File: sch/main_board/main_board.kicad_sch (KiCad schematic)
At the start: 58 parts, among them J1 BVCC, J13 5V_GND, J14 IO23, J15 IO22, J16 IO1, J17 IO3, J18 IO21, J2 BGND, J21 5V, J22 TX2, J23 RX2, J24 12V_CUT2, J25 12V_CUT, J26 DC 12V, J27 DC 5V, J3 3.3V, J30 5V_CUT, J4 PWR_MOTOR_L, J5 PWR_MOTOR_R, J6 CUT_LOAD, J7 MOTOR_L, J8 MOTOR_R, J9 EN, Q1 BC847, Q2 K4145, Q3 K4145, Q4 BC847, Q5 K4145, Q6 BC847, Q7 K4145, Q8 BC847, Q9 K4145

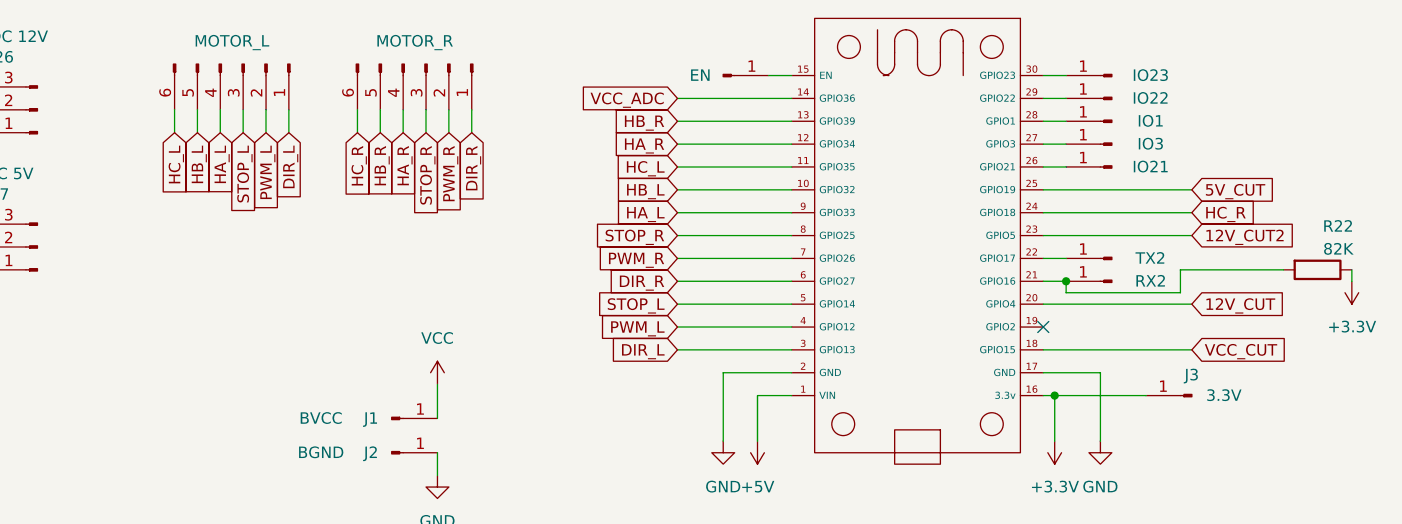
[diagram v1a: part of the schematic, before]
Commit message: Swap the motors. Simply because it easier to connect
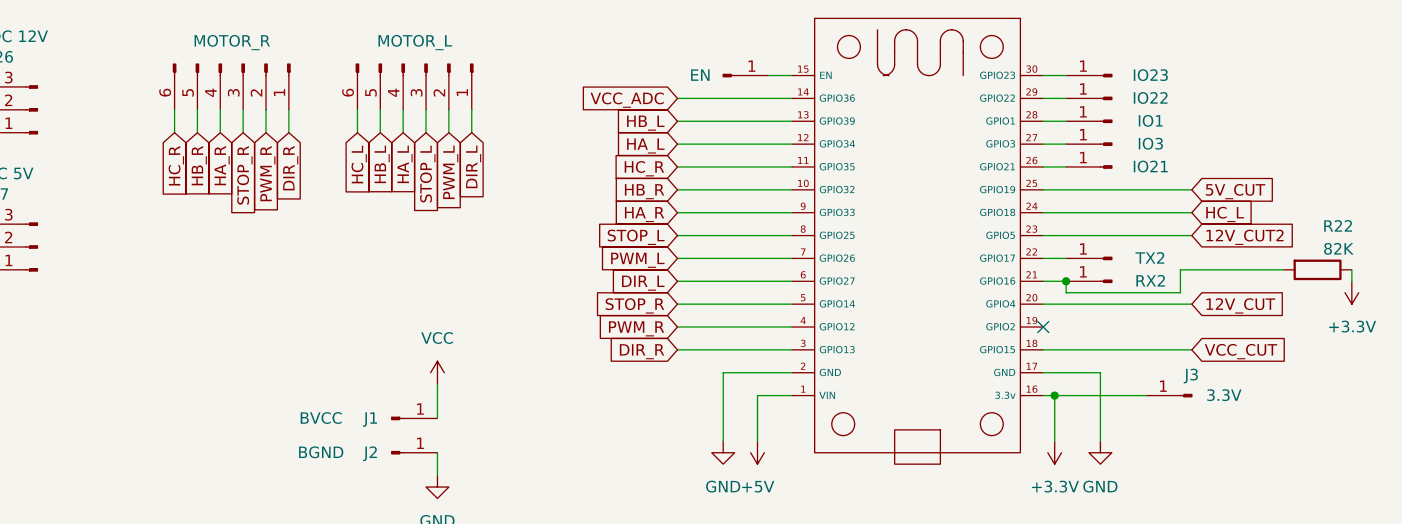
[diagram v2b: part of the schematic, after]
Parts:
- J7: value MOTOR_L -> MOTOR_R
- J8: value MOTOR_R -> MOTOR_L
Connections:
- net DIR_L: now also J8.1 (Pin_1), U1.6 (GPIO27); no longer J7.1 (Pin_1), U1.3 (GPIO13)
- net DIR_R: now also J7.1 (Pin_1), U1.3 (GPIO13); no longer J8.1 (Pin_1), U1.6 (GPIO27)
- net HA_L: now also J8.4 (Pin_4), U1.12 (GPIO34); no longer J7.4 (Pin_4), U1.9 (GPIO33)
- net HA_R: now also J7.4 (Pin_4), U1.9 (GPIO33); no longer J8.4 (Pin_4), U1.12 (GPIO34)
- net HB_L: now also J8.5 (Pin_5), U1.13 (GPIO39); no longer J7.5 (Pin_5), U1.10 (GPIO32)
- net HB_R: now also J7.5 (Pin_5), U1.10 (GPIO32); no longer J8.5 (Pin_5), U1.13 (GPIO39)
- net HC_L: now also J8.6 (Pin_6), U1.24 (GPIO18); no longer J7.6 (Pin_6), U1.11 (GPIO35)
- net HC_R: now also J7.6 (Pin_6), U1.11 (GPIO35); no longer J8.6 (Pin_6), U1.24 (GPIO18)
- net PWM_L: now also J8.2 (Pin_2), U1.7 (GPIO26); no longer J7.2 (Pin_2), U1.4 (GPIO12)
- net PWM_R: now also J7.2 (Pin_2), U1.4 (GPIO12); no longer J8.2 (Pin_2), U1.7 (GPIO26)
- net STOP_L: now also J8.3 (Pin_3), U1.8 (GPIO25); no longer J7.3 (Pin_3), U1.5 (GPIO14)
- net STOP_R: now also J7.3 (Pin_3), U1.5 (GPIO14); no longer J8.3 (Pin_3), U1.8 (GPIO25)
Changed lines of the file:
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@@
 		)
 	)
-	(global_label "HA_R"
+	(global_label "HA_L"
 		(shape input)
 		(at 205.74 29.21 180)
@@
 		)
 		(property "Intersheetrefs" "${INTERSHEET_REFS}"
-			(at 198.0981 29.21 0)
+			(at 198.34 29.21 0)
 			(effects
 				(font
@@
 		)
 	)
-	(global_label "PWM_R"
+	(global_label "PWM_L"
 		(shape input)
 		(at 180.34 27.94 270)
@@
 		)
 		(property "Intersheetrefs" "${INTERSHEET_REFS}"
-			(at 180.34 37.3356 90)
+			(at 180.34 37.0937 90)
 			(effects
 				(font
@@
 		)
 	)
-	(global_label "HC_R"
+	(global_label "HC_L"
 		(shape input)
 		(at 262.89 36.83 0)
@@
 		)
 		(property "Intersheetrefs" "${INTERSHEET_REFS}"
-			(at 270.7133 36.83 0)
+			(at 270.4714 36.83 0)
 			(effects
 				(font
@@
 		)
 	)
-	(global_label "DIR_R"
+	(global_label "DIR_L"
 		(shape input)
 		(at 182.88 27.94 270)
@@
 		)
 		(property "Intersheetrefs" "${INTERSHEET_REFS}"
-			(at 182.88 36.3076 90)
+			(at 182.88 36.0657 90)
 			(effects
 				(font
@@
 		)
 	)
-	(global_label "HC_L"
+	(global_label "HC_R"
 		(shape input)
 		(at 205.74 31.75 180)
@@
 		)
 		(property "Intersheetrefs" "${INTERSHEET_REFS}"
-			(at 198.1586 31.75 0)
+			(at 197.9167 31.75 0)
 			(effects
 				(font
@@
 		)
 	)
-	(global_label "HC_L"
+	(global_label "HC_R"
 		(shape input)
 		(at 149.86 27.94 270)
@@
 		)
 		(property "Intersheetrefs" "${INTERSHEET_REFS}"
-			(at 149.86 35.5214 90)
+			(at 149.86 35.7633 90)
 			(effects
 				(font
@@
 		)
 	)
-	(global_label "PWM_L"
+	(global_label "PWM_R"
 		(shape input)
 		(at 205.74 49.53 180)
@@
 		)
 		(property "Intersheetrefs" "${INTERSHEET_REFS}"
-			(at 196.5863 49.53 0)
+			(at 196.3444 49.53 0)
 			(effects
 				(font
@@
 		)
 	)
-	(global_label "HB_R"
+	(global_label "HB_L"
 		(shape input)
 		(at 205.74 26.67 180)
@@
 		)
 		(property "Intersheetrefs" "${INTERSHEET_REFS}"
-			(at 197.9167 26.67 0)
+			(at 198.1586 26.67 0)
 			(effects
 				(font
@@
 		)
 	)
-	(global_label "PWM_R"
+	(global_label "PWM_L"
 		(shape input)
 		(at 205.74 41.91 180)
@@
 		)
 		(property "Intersheetrefs" "${INTERSHEET_REFS}"
-			(at 196.3444 41.91 0)
+			(at 196.5863 41.91 0)
 			(effects
 				(font
@@
 		)
 	)
-	(global_label "DIR_L"
+	(global_label "DIR_R"
 		(shape input)
 		(at 162.56 27.94 270)
@@
 		)
 		(property "Intersheetrefs" "${INTERSHEET_REFS}"
-			(at 162.56 36.0657 90)
+			(at 162.56 36.3076 90)
 			(effects
 				(font
@@
 		)
 	)
-	(global_label "HA_L"
+	(global_label "HA_R"
 		(shape input)
 		(at 205.74 36.83 180)
@@
 		)
 		(property "Intersheetrefs" "${INTERSHEET_REFS}"
-			(at 198.34 36.83 0)
+			(at 198.0981 36.83 0)
 			(effects
 				(font
@@
 		)
 	)
-	(global_label "HA_R"
+	(global_label "HA_L"
 		(shape input)
 		(at 175.26 27.94 270)
@@
 		)
 		(property "Intersheetrefs" "${INTERSHEET_REFS}"
-			(at 175.26 35.5819 90)
+			(at 175.26 35.34 90)
 			(effects
 				(font
@@
 		)
 	)
-	(global_label "HB_R"
+	(global_label "HB_L"
 		(shape input)
 		(at 172.72 27.94 270)
@@
 		)
 		(property "Intersheetrefs" "${INTERSHEET_REFS}"
-			(at 172.72 35.7633 90)
+			(at 172.72 35.5214 90)
 			(effects
 				(font
@@
 		)
 	)
-	(global_label "HB_L"
+	(global_label "HB_R"
 		(shape input)
 		(at 205.74 34.29 180)
@@
 		)
 		(property "Intersheetrefs" "${INTERSHEET_REFS}"
-			(at 198.1586 34.29 0)
+			(at 197.9167 34.29 0)
 			(effects
 				(font
@@
 		)
 	)
-	(global_label "STOP_R"
+	(global_label "STOP_L"
 		(shape input)
 		(at 177.8 27.94 270)
@@
 		)
 		(property "Intersheetrefs" "${INTERSHEET_REFS}"
-			(at 177.8 37.9404 90)
+			(at 177.8 37.6985 90)
 			(effects
 				(font
@@
 		)
 	)
-	(global_label "STOP_L"
+	(global_label "STOP_R"
 		(shape input)
 		(at 205.74 46.99 180)
@@
 		)
 		(property "Intersheetrefs" "${INTERSHEET_REFS}"
-			(at 195.9815 46.99 0)
+			(at 195.7396 46.99 0)
 			(effects
 				(font
@@
 		)
 	)
-	(global_label "HB_L"
+	(global_label "HB_R"
 		(shape input)
 		(at 152.4 27.94 270)
@@
 		)
 		(property "Intersheetrefs" "${INTERSHEET_REFS}"
-			(at 152.4 35.5214 90)
+			(at 152.4 35.7633 90)
 			(effects
 				(font
@@
 		)
 	)
-	(global_label "PWM_L"
+	(global_label "PWM_R"
 		(shape input)
 		(at 160.02 27.94 270)
@@
 		)
 		(property "Intersheetrefs" "${INTERSHEET_REFS}"
-			(at 160.02 37.0937 90)
+			(at 160.02 37.3356 90)
 			(effects
 				(font
@@
 		)
 	)
-	(global_label "DIR_R"
+	(global_label "DIR_L"
 		(shape input)
 		(at 205.74 44.45 180)
@@
 		)
 		(property "Intersheetrefs" "${INTERSHEET_REFS}"
-			(at 197.3724 44.45 0)
+			(at 197.6143 44.45 0)
 			(effects
 				(font
@@
 		)
 	)
-	(global_label "STOP_R"
+	(global_label "STOP_L"
 		(shape input)
 		(at 205.74 39.37 180)
@@
 		)
 		(property "Intersheetrefs" "${INTERSHEET_REFS}"
-			(at 195.7396 39.37 0)
+			(at 195.9815 39.37 0)
 			(effects
 				(font
@@
 		)
 	)
-	(global_label "STOP_L"
+	(global_label "STOP_R"
 		(shape input)
 		(at 157.48 27.94 270)
@@
 		)
 		(property "Intersheetrefs" "${INTERSHEET_REFS}"
-			(at 157.48 37.6985 90)
+			(at 157.48 37.9404 90)
 			(effects
 				(font
@@
 		)
 	)
-	(global_label "HC_R"
+	(global_label "HC_L"
 		(shape input)
 		(at 170.18 27.94 270)
@@
 		)
 		(property "Intersheetrefs" "${INTERSHEET_REFS}"
-			(at 170.18 35.7633 90)
+			(at 170.18 35.5214 90)
 			(effects
 				(font
@@
 		)
 	)
-	(global_label "HA_L"
+	(global_label "HA_R"
 		(shape input)
 		(at 154.94 27.94 270)
@@
 		)
 		(property "Intersheetrefs" "${INTERSHEET_REFS}"
-			(at 154.94 35.34 90)
+			(at 154.94 35.5819 90)
 			(effects
 				(font
@@
 		)
 	)
-	(global_label "DIR_L"
+	(global_label "DIR_R"
 		(shape input)
 		(at 205.74 52.07 180)
@@
 		)
 		(property "Intersheetrefs" "${INTERSHEET_REFS}"
-			(at 197.6143 52.07 0)
+			(at 197.3724 52.07 0)
 			(effects
 				(font
@@
 			)
 		)
-		(property "Value" "MOTOR_R"
+		(property "Value" "MOTOR_L"
 			(at 176.53 17.78 90)
 			(effects
@@
 			)
 		)
-		(property "Value" "MOTOR_L"
+		(property "Value" "MOTOR_R"
 			(at 156.21 17.78 90)
 			(effects

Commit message: Final scheme changes before production
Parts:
- removed C1: 1uf, Capacitor_SMD:C_0805_2012Metric_Pad1.18x1.45mm_HandSolder, symbol Device:C
- removed D1, D2: D, Diode_SMD:D_SMA_Handsoldering, symbol Device:D
- removed Q1, Q4, Q6, Q8: BC847, Package_TO_SOT_SMD:SOT-23, symbol Transistor_BJT:BC847
- removed Q2, Q3, Q5, Q7, Q9: K4145, Package_TO_SOT_THT:TO-220-3_Vertical, symbol Transistor_FET:Q_NMOS_GDS
- removed R15: 10K, Resistor_SMD:R_0805_2012Metric, symbol Device:R
- removed R16, R17, R2: 100K, Resistor_SMD:R_0805_2012Metric, symbol Device:R
- removed R18: 680, Resistor_SMD:R_0805_2012Metric, symbol Device:R
- removed R21: 100, Resistor_SMD:R_0805_2012Metric, symbol Device:R
- added D1, D2: 5.1, Diode_THT:D_5W_P12.70mm_Horizontal, symbol Device:D_Zener
- added D3, D4, D5, D6: D, Diode_SMD:D_2010_5025Metric_Pad1.52x2.65mm_HandSolder, symbol Device:D
- added Q1, Q2, Q3, Q4, Q5: IRF4905, Package_TO_SOT_THT:TO-220-3_Vertical, symbol Transistor_FET:Q_PMOS_GDS
- added R3: 820, Resistor_SMD:R_0805_2012Metric, symbol Device:R
- added U2, U3, U4, U5: EL817, Package_DIP:SMDIP-4_W9.53mm, symbol Isolator:EL817
- R1: value 10K -> 20K
- R10: value 680 -> 1
- R11: value 10K -> 1
- R12, R13: value 100K -> 680
- R2: renamed from R3; value 100K -> 68K
- R4: value 680 -> 820
- R5: value 1 -> 68K
- R6: value 1 -> 820
- R7: value 10K -> 68K
- R8: value 100K -> 820
- R9: value 100K -> 68K
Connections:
- net +12V: now also Q2.3 (S), Q3.3 (S); no longer J24.2 (Pin_2), J25.2 (Pin_2)
- net +3.3V: no longer R12.2, R8.2
- net +5V: now also Q4.3 (S); no longer J21.1 (Pin_1), J30.2 (Pin_2)
- net 12V_CUT: now also R4.2; no longer R11.1
- net 12V_CUT2: now also R6.2
- net 5V_CUT: now also R8.2; no longer R7.1
- net GND: now also J13.1 (Pin_1), J24.1 (Pin_1), J25.1 (Pin_1), J26.2 (Pin_2), J27.2 (Pin_2), J30.1 (Pin_1), J4.1 (Pin_1), J5.1 (Pin_1), J6.1 (Pin_1), R1.1, D3.2 (A), D4.2 (A), D5.2 (A), D6.2 (A), U2.2, U3.2, U3.3, U4.2, U4.3, U5.2, U5.3; no longer J26.1 (Pin_1), J27.1 (Pin_1)
- net VCC: now also J26.1 (Pin_1), J27.1 (Pin_1), R2.2, R5.2, R7.2, R9.2, D1.1 (K), Q1.3 (S), Q5.3 (S); no longer J26.2 (Pin_2), J27.2 (Pin_2), J4.2 (Pin_2), J5.2 (Pin_2), J6.2 (Pin_2)
- net VCC_CUT: now also R3.2; no longer R1.1
- net at R8.1: now also U5.1; no longer R7.2
- net at R12.1: now also Q4.1 (G); no longer R11.2
- net MF_GND: now reaches R1.2
- net MF_GND: now also D2.2 (A), U2.3
- net at R4.1: now also U3.1; no longer R2.1
- net at R14.1: now also Q3.1 (G); no longer R13.1
- net at R14.2: now also R7.1, U4.4
- net at R9.1: now also R12.2, U5.4; no longer R10.1
- net at R10.2: now also R11.2, R2.1, U2.4
- removed net MF_VCC: R13.2, R2.2, R9.2
- new net: D3.1 (K), J4.2 (Pin_2), J5.2 (Pin_2), J6.2 (Pin_2), Q1.2 (D), Q5.2 (D)
- new net: D4.1 (K), J21.1 (Pin_1), J30.2 (Pin_2), Q4.2 (D)
- new net: D6.1 (K), J24.2 (Pin_2), Q3.2 (D)
- new net: Q5.1 (G), R11.1
- new net: D1.2 (A), D2.1 (K)
- new net: R13.2, R5.1, U3.4
- new net: Q2.1 (G), R13.1
- new net: Q1.1 (G), R10.1
- new net: D5.1 (K), J25.2 (Pin_2), Q2.2 (D)
- new net: R3.1, U2.1
- new net: R6.1, U4.1
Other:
- moved on the sheet: J1, J13, J2, J21, J24, J25, J30, R2
